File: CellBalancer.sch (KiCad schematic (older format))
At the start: 8 parts, among them IC1 MAX923, Q1 IRF7455PBF

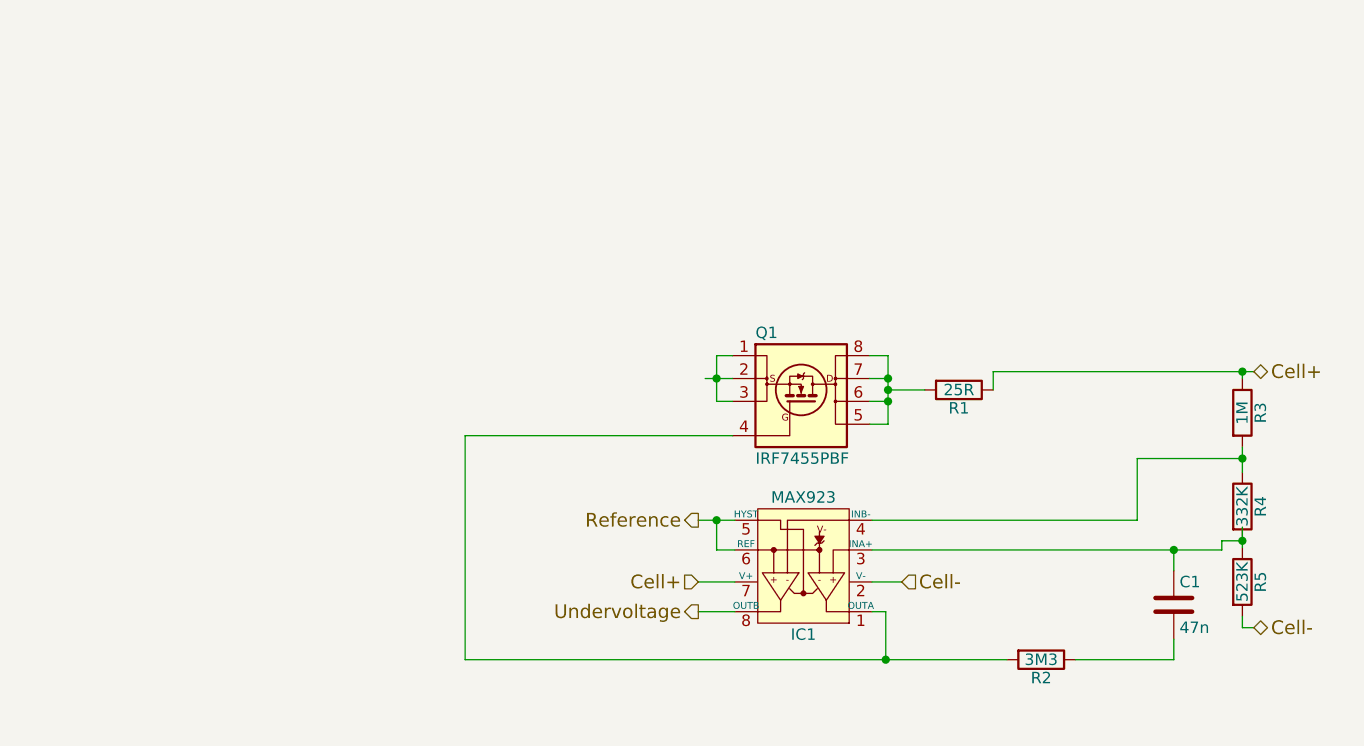
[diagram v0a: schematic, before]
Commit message: high voltage protection done
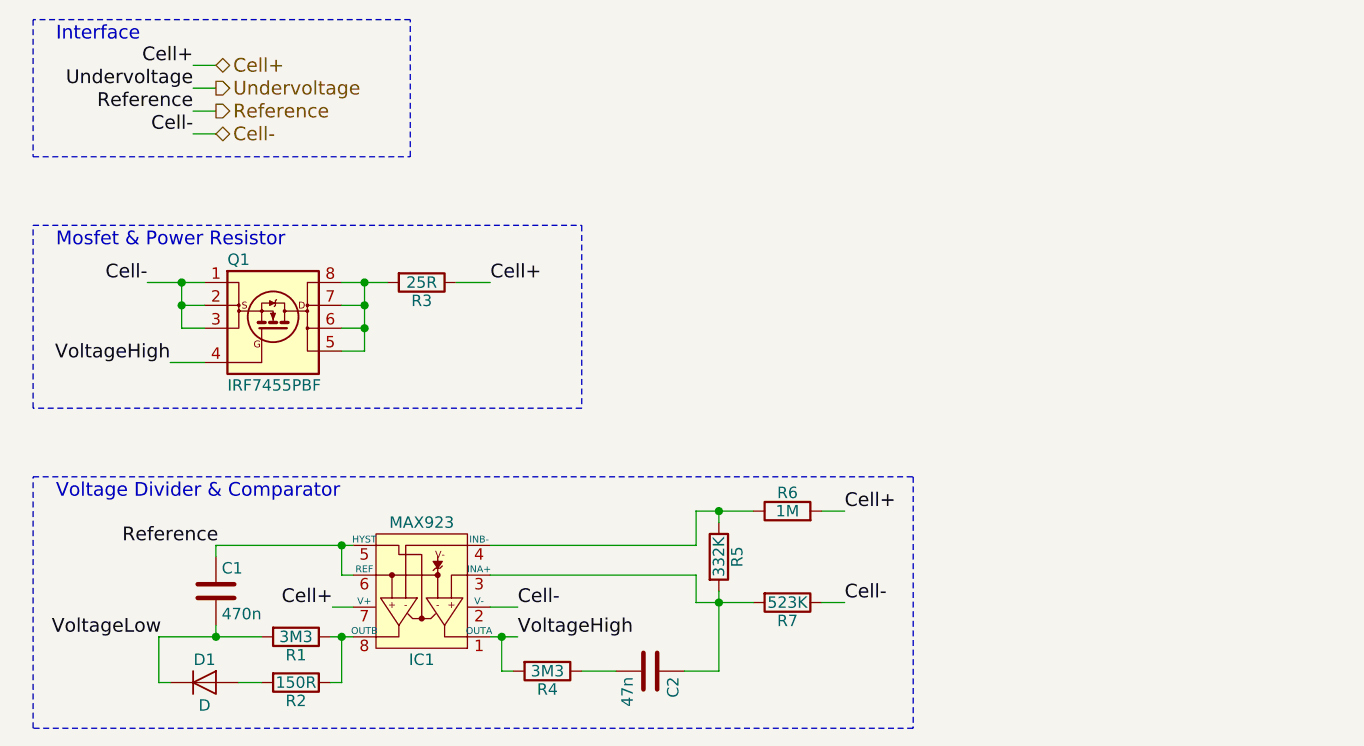
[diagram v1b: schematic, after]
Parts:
- removed R3: 1M, symbol R
- added C2: 47n, symbol C
- added D1: D, symbol D
- added R1: 3M3, symbol R
- added R6: 1M, symbol R
- added R7: 523K, symbol R
- C1: value 47n -> 470n
- R2: value 3M3 -> 150R
- R4: value 332K -> 3M3
- R5: value 523K -> 332K
- renumbered R1 to R3
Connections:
- net labels added: VoltageHigh, VoltageLow
- wire segments 37 -> 44
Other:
- note added: "Interface"
- note added: "Mosfet & Power Resistor"
- note added: "Voltage Divider & Comparator"
- moved on the sheet: Q1, R3

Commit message: schematic done
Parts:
- renumbered IC1 to IC2, R1 to R3, R2 to R4, R3 to R5, R4 to R6, R5 to R7, R6 to R8, R7 to R9
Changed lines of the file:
@@
 $Descr A4 11693 8268
 encoding utf-8
-Sheet 2 4
+Sheet 4 4
 Title "Balancer"
 Date "2017-03-18"
@@
 Reference
 Text HLabel 1900 1100 2    60   Output ~ 0
-Undervoltage
+VoltageLow
 $Comp
 L IRF7455PBF Q1
@@
 AR Path="/58CDE720/58CDB997" Ref="Q2"  Part="1"
 AR Path="/58CDEEA6/58CDB997" Ref="Q3"  Part="1"
-F 0 "Q1" H 1950 2450 50  0000 L CNN
+F 0 "Q3" H 1950 2450 50  0000 L CNN
 F 1 "IRF7455PBF" H 1950 1900 50  0000 L CNN
 F 2 "Housings_SOIC:SOIC-8_3.9x4.9mm_Pitch1.27mm" H 2160 1740 50  0001 C CIN
@@
 $EndComp
 $Comp
-L R R3
+L R R5
 U 1 1 58CDB9A6
 P 2800 1950
-AR Path="/58CDDC72/58CDB9A6" Ref="R3"  Part="1"
-AR Path="/58CDE720/58CDB9A6" Ref="R10"  Part="1"
-AR Path="/58CDEEA6/58CDB9A6" Ref="R17"  Part="1"
-F 0 "R3" V 2880 1950 50  0000 C CNN
+AR Path="/58CDDC72/58CDB9A6" Ref="R5"  Part="1"
+AR Path="/58CDE720/58CDB9A6" Ref="R12"  Part="1"
+AR Path="/58CDEEA6/58CDB9A6" Ref="R19"  Part="1"
+F 0 "R19" V 2880 1950 50  0000 C CNN
 F 1 "25R" V 2800 1950 50  0000 C CNN
 F 2 "" V 2730 1950 50  0001 C CNN
@@
 $EndComp
 $Comp
-L R R6
+L R R8
 U 1 1 58CD80F2
 P 4400 2950
-AR Path="/58CDDC72/58CD80F2" Ref="R6"  Part="1"
-AR Path="/58CDE720/58CD80F2" Ref="R13"  Part="1"
-AR Path="/58CDEEA6/58CD80F2" Ref="R20"  Part="1"
-F 0 "R6" V 4480 2950 50  0000 C CNN
+AR Path="/58CDDC72/58CD80F2" Ref="R8"  Part="1"
+AR Path="/58CDE720/58CD80F2" Ref="R15"  Part="1"
+AR Path="/58CDEEA6/58CD80F2" Ref="R22"  Part="1"
+F 0 "R22" V 4480 2950 50  0000 C CNN
 F 1 "1M" V 4400 2950 50  0000 C CNN
 F 2 "" V 4330 2950 50  0001 C CNN
@@
 $EndComp
 $Comp
-L R R5
+L R R7
 U 1 1 58CD8143
 P 4100 3150
-AR Path="/58CDDC72/58CD8143" Ref="R5"  Part="1"
-AR Path="/58CDE720/58CD8143" Ref="R12"  Part="1"
-AR Path="/58CDEEA6/58CD8143" Ref="R19"  Part="1"
-F 0 "R5" V 4180 3150 50  0000 C CNN
+AR Path="/58CDDC72/58CD8143" Ref="R7"  Part="1"
+AR Path="/58CDE720/58CD8143" Ref="R14"  Part="1"
+AR Path="/58CDEEA6/58CD8143" Ref="R21"  Part="1"
+F 0 "R21" V 4180 3150 50  0000 C CNN
 F 1 "332K" V 4100 3150 50  0000 C CNN
 F 2 "" V 4030 3150 50  0001 C CNN
@@
 $EndComp
 $Comp
-L R R7
+L R R9
 U 1 1 58CD819C
 P 4400 3350
-AR Path="/58CDDC72/58CD819C" Ref="R7"  Part="1"
-AR Path="/58CDE720/58CD819C" Ref="R14"  Part="1"
-AR Path="/58CDEEA6/58CD819C" Ref="R21"  Part="1"
-F 0 "R7" V 4480 3350 50  0000 C CNN
+AR Path="/58CDDC72/58CD819C" Ref="R9"  Part="1"
+AR Path="/58CDE720/58CD819C" Ref="R16"  Part="1"
+AR Path="/58CDEEA6/58CD819C" Ref="R23"  Part="1"
+F 0 "R23" V 4480 3350 50  0000 C CNN
 F 1 "523K" V 4400 3350 50  0000 C CNN
 F 2 "" V 4330 3350 50  0001 C CNN
@@
 Cell+
 $Comp
-L MAX923 IC1
+L MAX923 IC2
 U 1 1 58CD8827
 P 2800 3300
-AR Path="/58CDDC72/58CD8827" Ref="IC1"  Part="1"
-AR Path="/58CDE720/58CD8827" Ref="IC2"  Part="1"
-AR Path="/58CDEEA6/58CD8827" Ref="IC3"  Part="1"
-F 0 "IC1" H 2800 3600 50  0000 C CNN
+AR Path="/58CDDC72/58CD8827" Ref="IC2"  Part="1"
+AR Path="/58CDE720/58CD8827" Ref="IC3"  Part="1"
+AR Path="/58CDEEA6/58CD8827" Ref="IC4"  Part="1"
+F 0 "IC4" H 2800 3600 50  0000 C CNN
 F 1 "MAX923" H 2800 3000 50  0000 C CNN
 F 2 "Housings_SOIC:SOIC-8_3.9x4.9mm_Pitch1.27mm" H 2810 2830 60  0001 C CIN
@@
 Cell-
 Text Label 1800 1100 2    60   ~ 0
-Undervoltage
+VoltageLow
 Text Label 1800 1200 2    60   ~ 0
 Reference
@@
 	2750 800  1100 800
 $Comp
-L R R4
+L R R6
 U 1 1 58CDBF0F
 P 3350 3650
-AR Path="/58CDDC72/58CDBF0F" Ref="R4"  Part="1"
-AR Path="/58CDE720/58CDBF0F" Ref="R11"  Part="1"
-AR Path="/58CDEEA6/58CDBF0F" Ref="R18"  Part="1"
-F 0 "R4" V 3430 3650 50  0000 C CNN
+AR Path="/58CDDC72/58CDBF0F" Ref="R6"  Part="1"
+AR Path="/58CDE720/58CDBF0F" Ref="R13"  Part="1"
+AR Path="/58CDEEA6/58CDBF0F" Ref="R20"  Part="1"
+F 0 "R20" V 3430 3650 50  0000 C CNN
 F 1 "3M3" V 3350 3650 50  0000 C CNN
 F 2 "" V 3280 3650 50  0001 C CNN
@@
 AR Path="/58CDE720/58CDBF54" Ref="C4"  Part="1"
 AR Path="/58CDEEA6/58CDBF54" Ref="C6"  Part="1"
-F 0 "C2" H 3825 3750 50  0000 L CNN
+F 0 "C6" H 3825 3750 50  0000 L CNN
 F 1 "47n" H 3825 3550 50  0000 L CNN
 F 2 "" H 3838 3500 50  0001 C CNN
@@
 Connection ~ 2450 3100
 $Comp
-L R R1
+L R R3
 U 1 1 58CDD170
 P 2250 3500
-AR Path="/58CDDC72/58CDD170" Ref="R1"  Part="1"
-AR Path="/58CDE720/58CDD170" Ref="R8"  Part="1"
-AR Path="/58CDEEA6/58CDD170" Ref="R15"  Part="1"
-F 0 "R1" V 2330 3500 50  0000 C CNN
+AR Path="/58CDDC72/58CDD170" Ref="R3"  Part="1"
+AR Path="/58CDE720/58CDD170" Ref="R10"  Part="1"
+AR Path="/58CDEEA6/58CDD170" Ref="R17"  Part="1"
+F 0 "R17" V 2330 3500 50  0000 C CNN
 F 1 "3M3" V 2250 3500 50  0000 C CNN
 F 2 "" V 2180 3500 50  0001 C CNN
@@
 $EndComp
 $Comp
-L R R2
+L R R4
 U 1 1 58CDD1EC
 P 2250 3700
-AR Path="/58CDDC72/58CDD1EC" Ref="R2"  Part="1"
-AR Path="/58CDE720/58CDD1EC" Ref="R9"  Part="1"
-AR Path="/58CDEEA6/58CDD1EC" Ref="R16"  Part="1"
-F 0 "R2" V 2330 3700 50  0000 C CNN
+AR Path="/58CDDC72/58CDD1EC" Ref="R4"  Part="1"
+AR Path="/58CDE720/58CDD1EC" Ref="R11"  Part="1"
+AR Path="/58CDEEA6/58CDD1EC" Ref="R18"  Part="1"
+F 0 "R18" V 2330 3700 50  0000 C CNN
 F 1 "150R" V 2250 3700 50  0000 C CNN
 F 2 "" V 2180 3700 50  0001 C CNN
@@
 AR Path="/58CDE720/58CDD221" Ref="D2"  Part="1"
 AR Path="/58CDEEA6/58CDD221" Ref="D3"  Part="1"
-F 0 "D1" H 1850 3800 50  0000 C CNN
+F 0 "D3" H 1850 3800 50  0000 C CNN
 F 1 "D" H 1850 3600 50  0000 C CNN
 F 2 "" H 1850 3700 50  0001 C CNN
@@
 AR Path="/58CDE720/58CDD43A" Ref="C3"  Part="1"
 AR Path="/58CDEEA6/58CDD43A" Ref="C5"  Part="1"
-F 0 "C1" H 1925 3400 50  0000 L CNN
+F 0 "C5" H 1925 3400 50  0000 L CNN
 F 1 "470n" H 1925 3200 50  0000 L CNN
 F 2 "" H 1938 3150 50  0001 C CNN

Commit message: added annotations
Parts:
- renumbered Q1 to Q2
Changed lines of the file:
@@
 VoltageLow
 $Comp
-L IRF7455PBF Q1
+L IRF7455PBF Q2
 U 1 1 58CDB997
 P 2150 2150
-AR Path="/58CDDC72/58CDB997" Ref="Q1"  Part="1"
-AR Path="/58CDE720/58CDB997" Ref="Q2"  Part="1"
-AR Path="/58CDEEA6/58CDB997" Ref="Q3"  Part="1"
-F 0 "Q3" H 1950 2450 50  0000 L CNN
+AR Path="/58CDDC72/58CDB997" Ref="Q2"  Part="1"
+AR Path="/58CDE720/58CDB997" Ref="Q3"  Part="1"
+AR Path="/58CDEEA6/58CDB997" Ref="Q4"  Part="1"
+F 0 "Q4" H 1950 2450 50  0000 L CNN
 F 1 "IRF7455PBF" H 1950 1900 50  0000 L CNN
 F 2 "Housings_SOIC:SOIC-8_3.9x4.9mm_Pitch1.27mm" H 2160 1740 50  0001 C CIN

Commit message: changed burner resistor to 22R, assigned all footprints
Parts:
- C1, C2: footprint (none) -> Capacitors_SMD:C_0805_HandSoldering
- D1: footprint (none) -> Diodes_SMD:D_0805
- R3, R4, R6, R7, R8, R9: footprint (none) -> Resistors_SMD:R_0805_HandSoldering
- R5: value 25R -> 22R; footprint (none) -> Resistors_SMD:R_0612
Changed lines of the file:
@@
 AR Path="/58CDEEA6/58CDB9A6" Ref="R19"  Part="1"
 F 0 "R19" V 2880 1950 50  0000 C CNN
-F 1 "25R" V 2800 1950 50  0000 C CNN
-F 2 "" V 2730 1950 50  0001 C CNN
+F 1 "22R" V 2800 1950 50  0000 C CNN
+F 2 "Resistors_SMD:R_0612" V 2730 1950 50  0001 C CNN
 F 3 "" H 2800 1950 50  0001 C CNN
 	1    2800 1950
@@
 F 0 "R22" V 4480 2950 50  0000 C CNN
 F 1 "1M" V 4400 2950 50  0000 C CNN
-F 2 "" V 4330 2950 50  0001 C CNN
+F 2 "Resistors_SMD:R_0805_HandSoldering" V 4330 2950 50  0001 C CNN
 F 3 "" H 4400 2950 50  0001 C CNN
 	1    4400 2950
@@
 F 0 "R21" V 4180 3150 50  0000 C CNN
 F 1 "332K" V 4100 3150 50  0000 C CNN
-F 2 "" V 4030 3150 50  0001 C CNN
+F 2 "Resistors_SMD:R_0805_HandSoldering" V 4030 3150 50  0001 C CNN
 F 3 "" H 4100 3150 50  0001 C CNN
 	1    4100 3150
@@
 F 0 "R23" V 4480 3350 50  0000 C CNN
 F 1 "523K" V 4400 3350 50  0000 C CNN
-F 2 "" V 4330 3350 50  0001 C CNN
+F 2 "Resistors_SMD:R_0805_HandSoldering" V 4330 3350 50  0001 C CNN
 F 3 "" H 4400 3350 50  0001 C CNN
 	1    4400 3350
@@
 F 0 "R20" V 3430 3650 50  0000 C CNN
 F 1 "3M3" V 3350 3650 50  0000 C CNN
-F 2 "" V 3280 3650 50  0001 C CNN
+F 2 "Resistors_SMD:R_0805_HandSoldering" V 3280 3650 50  0001 C CNN
 F 3 "" H 3350 3650 50  0001 C CNN
 	1    3350 3650
@@
 F 0 "C6" H 3825 3750 50  0000 L CNN
 F 1 "47n" H 3825 3550 50  0000 L CNN
-F 2 "" H 3838 3500 50  0001 C CNN
+F 2 "Capacitors_SMD:C_0805_HandSoldering" H 3838 3500 50  0001 C CNN
 F 3 "" H 3800 3650 50  0001 C CNN
 	1    3800 3650
@@
 F 0 "R17" V 2330 3500 50  0000 C CNN
 F 1 "3M3" V 2250 3500 50  0000 C CNN
-F 2 "" V 2180 3500 50  0001 C CNN
+F 2 "Resistors_SMD:R_0805_HandSoldering" V 2180 3500 50  0001 C CNN
 F 3 "" H 2250 3500 50  0001 C CNN
 	1    2250 3500
@@
 F 0 "R18" V 2330 3700 50  0000 C CNN
 F 1 "150R" V 2250 3700 50  0000 C CNN
-F 2 "" V 2180 3700 50  0001 C CNN
+F 2 "Resistors_SMD:R_0805_HandSoldering" V 2180 3700 50  0001 C CNN
 F 3 "" H 2250 3700 50  0001 C CNN
 	1    2250 3700
@@
 F 0 "D3" H 1850 3800 50  0000 C CNN
 F 1 "D" H 1850 3600 50  0000 C CNN
-F 2 "" H 1850 3700 50  0001 C CNN
+F 2 "Diodes_SMD:D_0805" H 1850 3700 50  0001 C CNN
 F 3 "" H 1850 3700 50  0001 C CNN
 	1    1850 3700
@@
 F 0 "C5" H 1925 3400 50  0000 L CNN
 F 1 "470n" H 1925 3200 50  0000 L CNN
-F 2 "" H 1938 3150 50  0001 C CNN
+F 2 "Capacitors_SMD:C_0805_HandSoldering" H 1938 3150 50  0001 C CNN
 F 3 "" H 1900 3300 50  0001 C CNN
 	1    1900 3300

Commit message: Front side pcb first version
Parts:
- C1, C2: footprint Capacitors_SMD:C_0805_HandSoldering -> Capacitors_SMD:C_0805
- R3, R4, R6, R7, R8, R9: footprint Resistors_SMD:R_0805_HandSoldering -> Resistors_SMD:R_0805
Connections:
- net VoltageHigh: now also R6.1; no longer R6.2
- net at IC2.4 (INB-), R8.1: now also R7.2; no longer R7.1
- net at IC2.3 (INA+), R9.2: now also C2.2, R7.1; no longer C2.1, R7.2
- new net: C2.1, R6.2
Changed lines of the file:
@@
 AR Path="/58CDE720/58CDB997" Ref="Q3"  Part="1"
 AR Path="/58CDEEA6/58CDB997" Ref="Q4"  Part="1"
-F 0 "Q4" H 1950 2450 50  0000 L CNN
+F 0 "Q2" H 1950 2450 50  0000 L CNN
 F 1 "IRF7455PBF" H 1950 1900 50  0000 L CNN
 F 2 "Housings_SOIC:SOIC-8_3.9x4.9mm_Pitch1.27mm" H 2160 1740 50  0001 C CIN
@@
 AR Path="/58CDE720/58CDB9A6" Ref="R12"  Part="1"
 AR Path="/58CDEEA6/58CDB9A6" Ref="R19"  Part="1"
-F 0 "R19" V 2880 1950 50  0000 C CNN
+F 0 "R5" V 2880 1950 50  0000 C CNN
 F 1 "22R" V 2800 1950 50  0000 C CNN
 F 2 "Resistors_SMD:R_0612" V 2730 1950 50  0001 C CNN
@@
 AR Path="/58CDE720/58CD80F2" Ref="R15"  Part="1"
 AR Path="/58CDEEA6/58CD80F2" Ref="R22"  Part="1"
-F 0 "R22" V 4480 2950 50  0000 C CNN
+F 0 "R8" V 4480 2950 50  0000 C CNN
 F 1 "1M" V 4400 2950 50  0000 C CNN
-F 2 "Resistors_SMD:R_0805_HandSoldering" V 4330 2950 50  0001 C CNN
+F 2 "Resistors_SMD:R_0805" V 4330 2950 50  0001 C CNN
 F 3 "" H 4400 2950 50  0001 C CNN
 	1    4400 2950
@@
 AR Path="/58CDE720/58CD8143" Ref="R14"  Part="1"
 AR Path="/58CDEEA6/58CD8143" Ref="R21"  Part="1"
-F 0 "R21" V 4180 3150 50  0000 C CNN
+F 0 "R7" V 4180 3150 50  0000 C CNN
 F 1 "332K" V 4100 3150 50  0000 C CNN
-F 2 "Resistors_SMD:R_0805_HandSoldering" V 4030 3150 50  0001 C CNN
+F 2 "Resistors_SMD:R_0805" V 4030 3150 50  0001 C CNN
 F 3 "" H 4100 3150 50  0001 C CNN
 	1    4100 3150
-	1    0    0    -1
+	1    0    0    1
 $EndComp
 $Comp
@@
 AR Path="/58CDE720/58CD819C" Ref="R16"  Part="1"
 AR Path="/58CDEEA6/58CD819C" Ref="R23"  Part="1"
-F 0 "R23" V 4480 3350 50  0000 C CNN
+F 0 "R9" V 4480 3350 50  0000 C CNN
 F 1 "523K" V 4400 3350 50  0000 C CNN
-F 2 "Resistors_SMD:R_0805_HandSoldering" V 4330 3350 50  0001 C CNN
+F 2 "Resistors_SMD:R_0805" V 4330 3350 50  0001 C CNN
 F 3 "" H 4400 3350 50  0001 C CNN
 	1    4400 3350
@@
 AR Path="/58CDE720/58CD8827" Ref="IC3"  Part="1"
 AR Path="/58CDEEA6/58CD8827" Ref="IC4"  Part="1"
-F 0 "IC4" H 2800 3600 50  0000 C CNN
+F 0 "IC2" H 2800 3600 50  0000 C CNN
 F 1 "MAX923" H 2800 3000 50  0000 C CNN
 F 2 "Housings_SOIC:SOIC-8_3.9x4.9mm_Pitch1.27mm" H 2810 2830 60  0001 C CIN
@@
 AR Path="/58CDE720/58CDBF0F" Ref="R13"  Part="1"
 AR Path="/58CDEEA6/58CDBF0F" Ref="R20"  Part="1"
-F 0 "R20" V 3430 3650 50  0000 C CNN
+F 0 "R6" V 3430 3650 50  0000 C CNN
 F 1 "3M3" V 3350 3650 50  0000 C CNN
-F 2 "Resistors_SMD:R_0805_HandSoldering" V 3280 3650 50  0001 C CNN
+F 2 "Resistors_SMD:R_0805" V 3280 3650 50  0001 C CNN
 F 3 "" H 3350 3650 50  0001 C CNN
 	1    3350 3650
-	0    1    1    0
+	0    -1   1    0
 $EndComp
 $Comp
@@
 AR Path="/58CDE720/58CDBF54" Ref="C4"  Part="1"
 AR Path="/58CDEEA6/58CDBF54" Ref="C6"  Part="1"
-F 0 "C6" H 3825 3750 50  0000 L CNN
+F 0 "C2" H 3825 3750 50  0000 L CNN
 F 1 "47n" H 3825 3550 50  0000 L CNN
-F 2 "Capacitors_SMD:C_0805_HandSoldering" H 3838 3500 50  0001 C CNN
+F 2 "Capacitors_SMD:C_0805" H 3838 3500 50  0001 C CNN
 F 3 "" H 3800 3650 50  0001 C CNN
 	1    3800 3650
-	0    1    1    0
+	0    -1   1    0
 $EndComp
 Wire Wire Line
@@
 AR Path="/58CDE720/58CDD170" Ref="R10"  Part="1"
 AR Path="/58CDEEA6/58CDD170" Ref="R17"  Part="1"
-F 0 "R17" V 2330 3500 50  0000 C CNN
+F 0 "R3" V 2330 3500 50  0000 C CNN
 F 1 "3M3" V 2250 3500 50  0000 C CNN
-F 2 "Resistors_SMD:R_0805_HandSoldering" V 2180 3500 50  0001 C CNN
+F 2 "Resistors_SMD:R_0805" V 2180 3500 50  0001 C CNN
 F 3 "" H 2250 3500 50  0001 C CNN
 	1    2250 3500
@@
 AR Path="/58CDE720/58CDD1EC" Ref="R11"  Part="1"
 AR Path="/58CDEEA6/58CDD1EC" Ref="R18"  Part="1"
-F 0 "R18" V 2330 3700 50  0000 C CNN
+F 0 "R4" V 2330 3700 50  0000 C CNN
 F 1 "150R" V 2250 3700 50  0000 C CNN
-F 2 "Resistors_SMD:R_0805_HandSoldering" V 2180 3700 50  0001 C CNN
+F 2 "Resistors_SMD:R_0805" V 2180 3700 50  0001 C CNN
 F 3 "" H 2250 3700 50  0001 C CNN
 	1    2250 3700
@@
 AR Path="/58CDE720/58CDD221" Ref="D2"  Part="1"
 AR Path="/58CDEEA6/58CDD221" Ref="D3"  Part="1"
-F 0 "D3" H 1850 3800 50  0000 C CNN
+F 0 "D1" H 1850 3800 50  0000 C CNN
 F 1 "D" H 1850 3600 50  0000 C CNN
 F 2 "Diodes_SMD:D_0805" H 1850 3700 50  0001 C CNN
@@
 AR Path="/58CDE720/58CDD43A" Ref="C3"  Part="1"
 AR Path="/58CDEEA6/58CDD43A" Ref="C5"  Part="1"
-F 0 "C5" H 1925 3400 50  0000 L CNN
+F 0 "C1" H 1925 3400 50  0000 L CNN
 F 1 "470n" H 1925 3200 50  0000 L CNN
-F 2 "Capacitors_SMD:C_0805_HandSoldering" H 1938 3150 50  0001 C CNN
+F 2 "Capacitors_SMD:C_0805" H 1938 3150 50  0001 C CNN
 F 3 "" H 1900 3300 50  0001 C CNN
 	1    1900 3300

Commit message: layout finalized
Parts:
- added D4: LED, LEDs:LED_0805, symbol LED
- added R24: 220R, Resistors_SMD:R_0805, symbol R
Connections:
- net Cell+: now also R5.2, R24.1; no longer R5.1
- net at Q2.5 (D), Q2.6 (D), Q2.7 (D)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: now also R5.1, D4.1 (K); no longer R5.2
- new net: D4.2 (A), R24.2
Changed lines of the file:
@@
 F 3 "" H 2800 1950 50  0001 C CNN
 	1    2800 1950
-	0    1    1    0
+	0    -1   1    0
 $EndComp
 $Comp
@@
 	2550 1950 2550 2250
 Wire Wire Line
-	2550 2250 2450 2250
+	2450 2250 2650 2250
 Connection ~ 2550 1950
 Wire Wire Line
@@
 Text Notes 1200 2900 0    60   ~ 0
 Voltage Divider & Comparator
+$Comp
+L R R24
+U 1 1 58CFD09E
+P 3200 2250
+AR Path="/58CDDC72/58CFD09E" Ref="R24"  Part="1"
+AR Path="/58CDE720/58CFD09E" Ref="R25"  Part="1"
+AR Path="/58CDEEA6/58CFD09E" Ref="R26"  Part="1"
+F 0 "R24" V 3280 2250 50  0000 C CNN
+F 1 "220R" V 3200 2250 50  0000 C CNN
+F 2 "Resistors_SMD:R_0805" V 3130 2250 50  0001 C CNN
+F 3 "" H 3200 2250 50  0001 C CNN
+	1    3200 2250
+	0    1    1    0
+$EndComp
+$Comp
+L LED D4
+U 1 1 58CFD291
+P 2800 2250
+AR Path="/58CDDC72/58CFD291" Ref="D4"  Part="1"
+AR Path="/58CDE720/58CFD291" Ref="D5"  Part="1"
+AR Path="/58CDEEA6/58CFD291" Ref="D6"  Part="1"
+F 0 "D4" H 2800 2350 50  0000 C CNN
+F 1 "LED" H 2800 2150 50  0000 C CNN
+F 2 "LEDs:LED_0805" H 2800 2250 50  0001 C CNN
+F 3 "" H 2800 2250 50  0001 C CNN
+	1    2800 2250
+	1    0    0    -1
+$EndComp
+Connection ~ 2550 2250
+Wire Wire Line
+	2950 2250 3050 2250
+Wire Wire Line
+	3010 1950 3010 2090
+Wire Wire Line
+	3010 2090 3440 2090
+Wire Wire Line
+	3440 2090 3440 2250
+Wire Wire Line
+	3440 2250 3350 2250
+Connection ~ 3010 1950
 $EndSCHEMATC

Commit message: added missing 3d models, recreated gerbers and drill files
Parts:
- D1: footprint Diodes_SMD:D_0805 -> balancer:D_0805
- R5: footprint Resistors_SMD:R_0612 -> balancer:R_0612
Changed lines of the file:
@@
 F 0 "R5" V 2880 1950 50  0000 C CNN
 F 1 "22R" V 2800 1950 50  0000 C CNN
-F 2 "Resistors_SMD:R_0612" V 2730 1950 50  0001 C CNN
+F 2 "balancer:R_0612" V 2730 1950 50  0001 C CNN
 F 3 "" H 2800 1950 50  0001 C CNN
 	1    2800 1950
@@
 F 0 "D1" H 1850 3800 50  0000 C CNN
 F 1 "D" H 1850 3600 50  0000 C CNN
-F 2 "Diodes_SMD:D_0805" H 1850 3700 50  0001 C CNN
+F 2 "balancer:D_0805" H 1850 3700 50  0001 C CNN
 F 3 "" H 1850 3700 50  0001 C CNN
 	1    1850 3700
